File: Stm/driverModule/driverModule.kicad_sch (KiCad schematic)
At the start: 19 parts, among them J101 Conn_02x13_Odd_Even, J102 AXK520147YG, J103 Conn_02x08_Odd_Even, J104 AXK520147YG, U102 ADM7171ACPZ-3.0-R7, U103 TJA1051T-3, U104 TPS5410DR, U105 SN74LV165APWR, U106 SN74LV165APWR

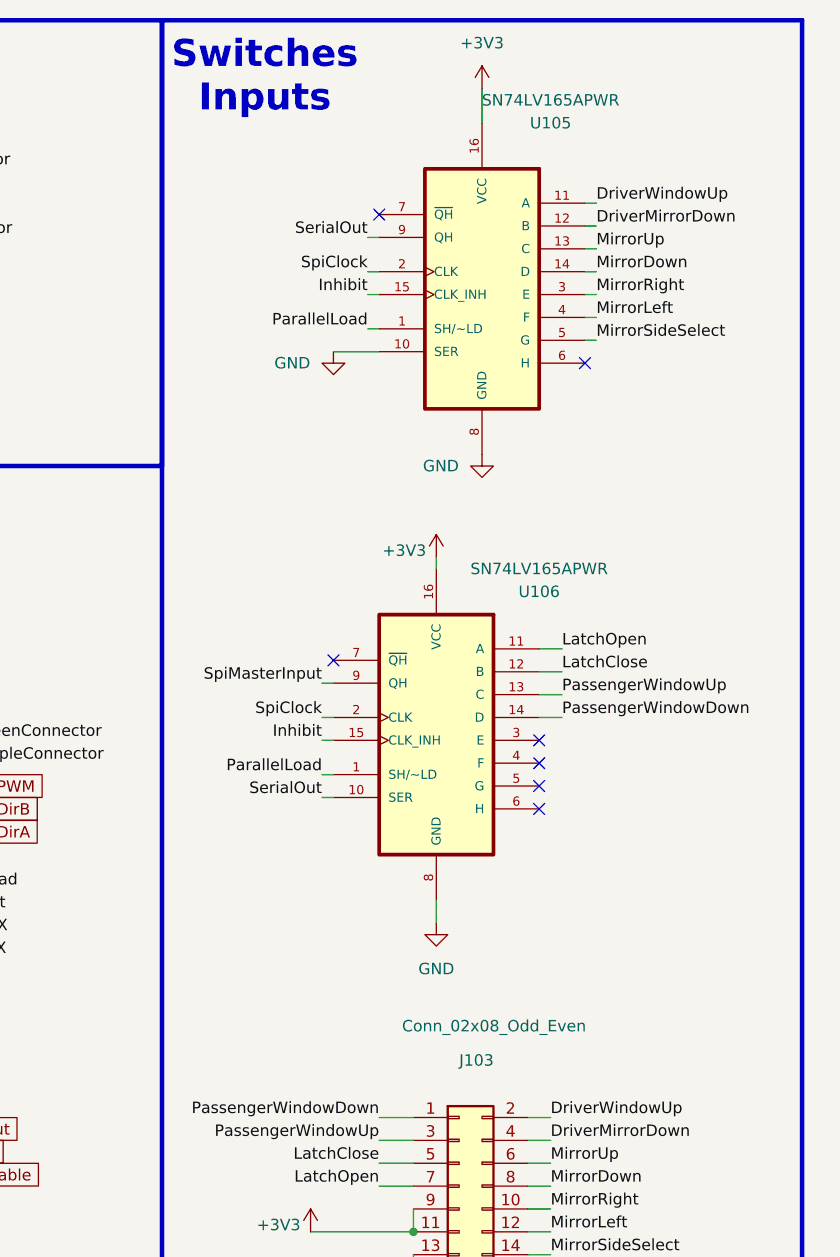
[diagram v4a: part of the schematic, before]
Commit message: Shift Registers
Changed shift registers to mc74hc165
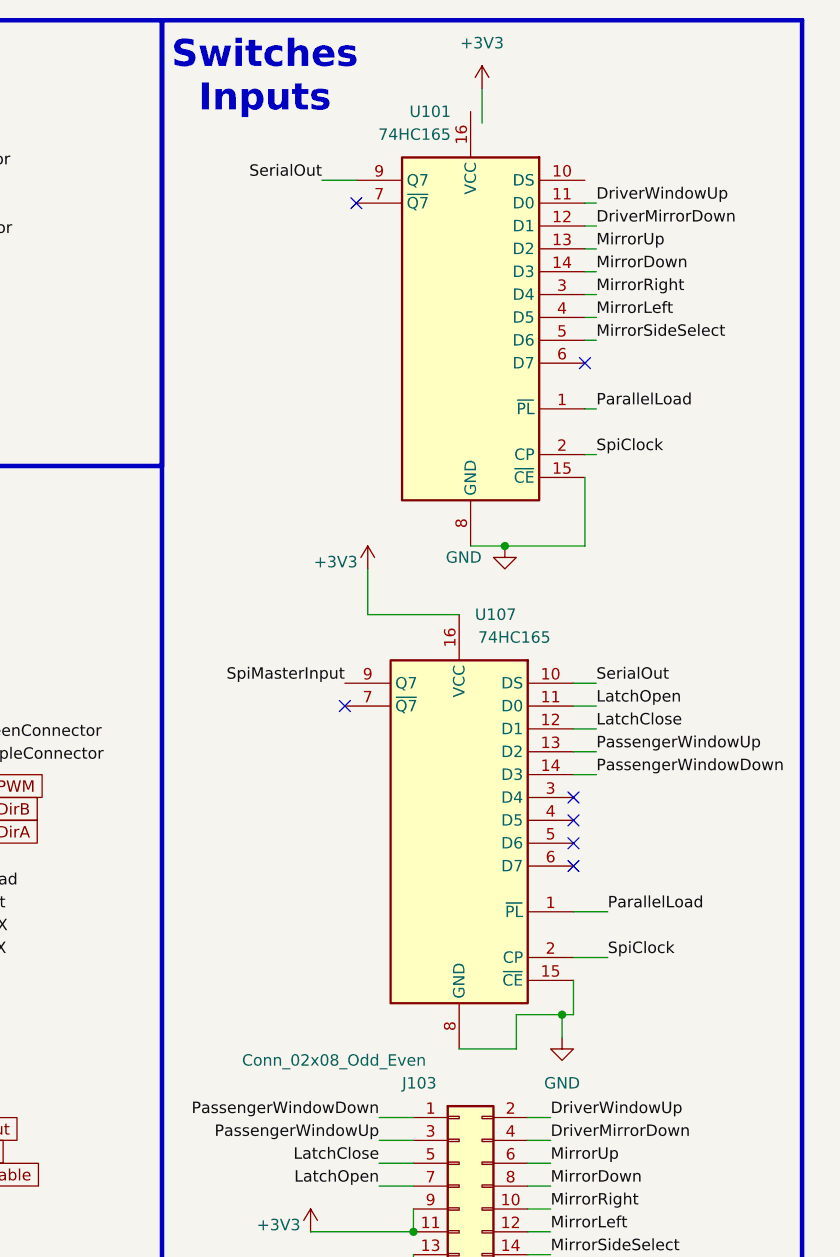
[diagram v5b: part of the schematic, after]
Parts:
- removed U105, U106: SN74LV165APWR, Package_SO:TSSOP-16_4.4x5mm_P0.65mm, symbol Local_symbols:SN74LV165APWR
- added U101, U107: 74HC165, symbol 74xx:74HC165
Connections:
- net +3V3: now also U107.16 (VCC)
- net DriverMirrorDown: now also U101.12 (D1)
- net DriverWindowUp: now also U101.11 (D0)
- net GND: now also U101.15 (~{CE}), U101.8 (GND), U107.15 (~{CE}), U107.8 (GND)
- net LatchClose: now also U107.12 (D1)
- net LatchOpen: now also U107.11 (D0)
- net MirrorDown: now also U101.14 (D3)
- net MirrorLeft: now also U101.4 (D5)
- net MirrorRight: now also U101.3 (D4)
- net MirrorSideSelect: now also U101.5 (D6)
- net MirrorUp: now also U101.13 (D2)
- net ParallelLoad: now also U101.1 (~{PL}), U107.1 (~{PL})
- net PassengerWindowDown: now also U107.14 (D3)
- net PassengerWindowUp: now also U107.13 (D2)
- net SerialOut: now also U101.9 (Q7), U107.10 (DS)
- net SpiClock: now also U101.2 (CP), U107.2 (CP)
- net SpiMasterInput: now also U107.9 (Q7)

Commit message: Symbols
Changed some symbols
Components placements
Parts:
- U101, U107: footprint (none) -> Package_SO:TSSOP-16_4.4x5mm_P0.65mm
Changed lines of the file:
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@@
 			)
 		)
-		(property "Footprint" ""
+		(property "Footprint" "Package_SO:TSSOP-16_4.4x5mm_P0.65mm"
 			(at 246.38 102.87 0)
 			(effects
@@
 			)
 		)
-		(property "Footprint" ""
+		(property "Footprint" "Package_SO:TSSOP-16_4.4x5mm_P0.65mm"
 			(at 247.65 46.99 0)
 			(effects

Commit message: 3d Models
Added Some 3d Models
And remove some components from schematic
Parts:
- J103, U101, U103, U107: now not fitted
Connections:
- net Inhibit is gone; now on net GND: J102.16
- net +3V3: now also U101.16 (VCC)
- no-connect marks 30 -> 31
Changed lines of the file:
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@@
 	)
 	(junction
-		(at 44.45 57.15)
-		(diameter 0)
-		(color 0 0 0 0)
-	)
-	(junction
 		(at 151.13 147.32)
 		(diameter 0)
@@
 	)
 	(no_connect
+		(at 260.35 31.75)
+	)
+	(no_connect
 		(at 259.08 100.33)
 	)
@@
 	(wire
 		(pts
+			(xy 176.53 111.76) (xy 199.39 111.76)
+		)
+		(stroke
+			(width 0)
+			(type default)
+		)
+	)
+	(wire
+		(pts
 			(xy 256.54 146.05) (xy 254 146.05)
 		)
@@
 	(wire
 		(pts
+			(xy 199.39 111.76) (xy 199.39 113.03)
+		)
+		(stroke
+			(width 0)
+			(type default)
+		)
+	)
+	(wire
+		(pts
 			(xy 55.88 90.17) (xy 54.61 90.17)
 		)
@@
 	(wire
 		(pts
-			(xy 248.92 21.59) (xy 248.92 25.4)
-		)
-		(stroke
-			(width 0)
-			(type default)
-		)
-	)
-	(wire
-		(pts
 			(xy 237.49 143.51) (xy 241.3 143.51)
 		)
@@
 	(wire
 		(pts
-			(xy 44.45 57.15) (xy 44.45 59.69)
-		)
-		(stroke
-			(width 0)
-			(type default)
-		)
-	)
-	(wire
-		(pts
 			(xy 147.32 114.3) (xy 147.32 115.57)
 		)
@@
 	(wire
 		(pts
-			(xy 236.22 80.01) (xy 246.38 80.01)
+			(xy 238.76 80.01) (xy 246.38 80.01)
 		)
 		(stroke
@@
 	(wire
 		(pts
-			(xy 190.5 113.03) (xy 176.53 113.03)
-		)
-		(stroke
-			(width 0)
-			(type default)
-		)
-	)
-	(wire
-		(pts
-			(xy 176.53 113.03) (xy 176.53 111.76)
-		)
-		(stroke
-			(width 0)
-			(type default)
-		)
-	)
-	(wire
-		(pts
 			(xy 185.42 115.57) (xy 189.23 115.57)
 		)
@@
 	(wire
 		(pts
-			(xy 45.72 57.15) (xy 44.45 57.15)
-		)
-		(stroke
-			(width 0)
-			(type default)
-		)
-	)
-	(wire
-		(pts
 			(xy 71.12 82.55) (xy 74.93 82.55)
 		)
@@
 	(wire
 		(pts
-			(xy 236.22 74.93) (xy 236.22 80.01)
+			(xy 238.76 78.74) (xy 238.76 80.01)
 		)
 		(stroke
@@
 	(wire
 		(pts
+			(xy 247.65 24.13) (xy 255.27 24.13)
+		)
+		(stroke
+			(width 0)
+			(type default)
+		)
+	)
+	(wire
+		(pts
 			(xy 49.53 59.69) (xy 44.45 59.69)
 		)
@@
 	(wire
 		(pts
+			(xy 255.27 24.13) (xy 255.27 22.86)
+		)
+		(stroke
+			(width 0)
+			(type default)
+		)
+	)
+	(wire
+		(pts
 			(xy 180.34 142.24) (xy 176.53 142.24)
 		)
@@
 	(wire
 		(pts
-			(xy 44.45 53.34) (xy 44.45 57.15)
+			(xy 44.45 53.34) (xy 44.45 59.69)
 		)
 		(stroke
@@
 		)
 	)
-	(label "EN"
-		(at 45.72 57.15 0)
-		(fields_autoplaced yes)
-		(effects
-			(font
-				(size 1.27 1.27)
-			)
-			(justify left bottom)
-		)
-	)
 	(label "MirrorSideSelect"
 		(at 256.54 151.13 0)
@@
 		)
 	)
-	(label "Inhibit"
-		(at 190.5 113.03 0)
-		(fields_autoplaced yes)
-		(effects
-			(font
-				(size 1.27 1.27)
-			)
-			(justify left bottom)
-		)
-	)
 	(label "ParallelLoad"
 		(at 186.69 110.49 0)
@@
 		(exclude_from_sim no)
 		(in_bom yes)
-		(on_board yes)
-		(dnp no)
+		(on_board no)
+		(dnp yes)
 		(fields_autoplaced yes)
 		(property "Reference" "U103"
@@
 		(exclude_from_sim no)
 		(in_bom yes)
-		(on_board yes)
-		(dnp no)
+		(on_board no)
+		(dnp yes)
 		(property "Reference" "U107"
 			(at 252.73 80.01 0)
@@
 		(exclude_from_sim no)
 		(in_bom yes)
-		(on_board yes)
-		(dnp no)
+		(on_board no)
+		(dnp yes)
 		(property "Reference" "U101"
 			(at 245.4559 24.13 0)
@@
 	)
 	(symbol
-		(lib_id "power:+3V3")
-		(at 248.92 21.59 0)
-		(unit 1)
-		(exclude_from_sim no)
-		(in_bom yes)
-		(on_board yes)
-		(dnp no)
-		(fields_autoplaced yes)
-		(property "Reference" "#PWR0120"
-			(at 248.92 25.4 0)
-			(effects
-				(font
-					(size 1.27 1.27)
-				)
-				(hide yes)
-			)
-		)
-		(property "Value" "+3V3"
-			(at 248.92 16.51 0)
-			(effects
-				(font
-					(size 1.27 1.27)
-				)
-			)
-		)
-		(property "Footprint" ""
-			(at 248.92 21.59 0)
-			(effects
-				(font
-					(size 1.27 1.27)
-				)
-				(hide yes)
-			)
-		)
-		(property "Datasheet" ""
-			(at 248.92 21.59 0)
-			(effects
-				(font
-					(size 1.27 1.27)
-				)
-				(hide yes)
-			)
-		)
-		(property "Description" "Power symbol creates a global label with name \"+3V3\""
-			(at 248.92 21.59 0)
-			(effects
-				(font
-					(size 1.27 1.27)
-				)
-				(hide yes)
-			)
-		)
-		(pin "1"
-		)
-		(instances
-			(project "driverModule"
-				(path "/959b66be-b3e0-42f8-ad58-f1baefc5b565"
-					(reference "#PWR0120")
-					(unit 1)
-				)
-			)
-		)
-	)
-	(symbol
 		(lib_id "power:GND")
 		(at 236.22 153.67 0)
@@
 	(symbol
 		(lib_id "power:+3V3")
-		(at 236.22 74.93 0)
+		(at 238.76 78.74 0)
 		(unit 1)
 		(exclude_from_sim no)
@@
 		(dnp no)
 		(property "Reference" "#PWR0122"
-			(at 236.22 78.74 0)
+			(at 238.76 82.55 0)
 			(effects
 				(font
@@
 		)
 		(property "Value" "+3V3"
-			(at 232.664 74.168 0)
+			(at 235.204 77.978 0)
 			(effects
 				(font
@@
 		)
 		(property "Footprint" ""
-			(at 236.22 74.93 0)
+			(at 238.76 78.74 0)
 			(effects
 				(font
@@
 		)
 		(property "Datasheet" ""
-			(at 236.22 74.93 0)
+			(at 238.76 78.74 0)
 			(effects
 				(font
@@
 		)
 		(property "Description" "Power symbol creates a global label with name \"+3V3\""
-			(at 236.22 74.93 0)
+			(at 238.76 78.74 0)
 			(effects
 				(font
@@
 	)
 	(symbol
+		(lib_id "power:GND")
+		(at 199.39 113.03 0)
+		(unit 1)
+		(exclude_from_sim no)
+		(in_bom yes)
+		(on_board yes)
+		(dnp no)
+		(property "Reference" "#PWR0131"
+			(at 199.39 119.38 0)
+			(effects
+				(font
+					(size 1.27 1.27)
+				)
+				(hide yes)
+			)
+		)
+		(property "Value" "GND"
+			(at 201.93 113.03 0)
+			(effects
+				(font
+					(size 1.27 1.27)
+				)
+			)
+		)
+		(property "Footprint" ""
+			(at 199.39 113.03 0)
+			(effects
+				(font
+					(size 1.27 1.27)
+				)
+				(hide yes)
+			)
+		)
+		(property "Datasheet" ""
+			(at 199.39 113.03 0)
+			(effects
+				(font
+					(size 1.27 1.27)
+				)
+				(hide yes)
+			)
+		)
+		(property "Description" "Power symbol creates a global label with name \"GND\" , ground"
+			(at 199.39 113.03 0)
+			(effects
+				(font
+					(size 1.27 1.27)
+				)
+				(hide yes)
+			)
+		)
+		(pin "1"
+		)
+		(instances
+			(project "driverModule"
+				(path "/959b66be-b3e0-42f8-ad58-f1baefc5b565"
+					(reference "#PWR0131")
+					(unit 1)
+				)
+			)
+		)
+	)
+	(symbol
 		(lib_id "Local_symbols:ADM7171ACPZ-3.0-R7")
 		(at 57.15 48.26 0)
@@
 		(exclude_from_sim no)
 		(in_bom yes)
-		(on_board yes)
-		(dnp no)
+		(on_board no)
+		(dnp yes)
 		(property "Reference" "J103"
 			(at 240.03 132.08 0)
@@
 					(unit 1)
 				)
+			)
+		)
+	)
+	(symbol
+		(lib_id "power:+3V3")
+		(at 255.27 22.86 0)
+		(unit 1)
+		(exclude_from_sim no)
+		(in_bom yes)
+		(on_board yes)
+		(dnp no)
+		(property "Reference" "#PWR0120"
+			(at 255.27 26.67 0)
+			(effects
+				(font
+					(size 1.27 1.27)
+				)
+				(hide yes)
+			)
+		)
+		(property "Value" "+3V3"
+			(at 251.714 22.098 0)
+			(effects
+				(font
+					(size 1.27 1.27)
+				)
+			)
+		)
+		(property "Footprint" ""
+			(at 255.27 22.86 0)
+			(effects
+				(font
+					(size 1.27 1.27)
+				)
+				(hide yes)
+			)
+		)
+		(property "Datasheet" ""
+			(at 255.27 22.86 0)
+			(effects
+				(font
+					(size 1.27 1.27)
+				)
+				(hide yes)
+			)
+		)
+		(property "Description" "Power symbol creates a global label with name \"+3V3\""
+			(at 255.27 22.86 0)
+			(effects
+				(font
+					(size 1.27 1.27)
+				)
+				(hide yes)
+			)
+		)
+		(pin "1"
+		)
+		(instances
+			(project "driverModule"
+				(path "/959b66be-b3e0-42f8-ad58-f1baefc5b565"
+					(reference "#PWR0120")
+					(unit 1)
+				)

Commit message: Routing
Finish some routing
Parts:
- added C1, C2, C3, C4: 0u1F, Capacitor_SMD:C_0402_1005Metric_Pad0.74x0.62mm_HandSolder, symbol Device:C
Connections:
- net +3V3: now also J103.5 (Pin_5), C1.1, C2.1, C3.1, C4.1; no longer J103.11 (Pin_11), J103.9 (Pin_9)
- net DriverWindowUp: now also J103.3 (Pin_3); no longer J103.2 (Pin_2)
- net GND: now also J103.12 (Pin_12), J103.14 (Pin_14), C1.2, C2.2, C3.2, C4.2; no longer J103.13 (Pin_13)
- net LatchClose: now also J103.11 (Pin_11); no longer J103.5 (Pin_5)
- net LatchOpen: now also J103.13 (Pin_13); no longer J103.7 (Pin_7)
- net MirrorDown: now also J103.2 (Pin_2); no longer J103.8 (Pin_8)
- net MirrorLeft: now also J103.7 (Pin_7); no longer J103.12 (Pin_12)
- net MirrorRight: now also J103.8 (Pin_8); no longer J103.10 (Pin_10)
- net MirrorSideSelect: now also J103.6 (Pin_6); no longer J103.14 (Pin_14)
- net MirrorUp: now also J103.1 (Pin_1); no longer J103.6 (Pin_6)
- net PassengerWindowDown: now also J103.9 (Pin_9); no longer J103.1 (Pin_1)
- net PassengerWindowUp: now also J103.10 (Pin_10); no longer J103.3 (Pin_3)
